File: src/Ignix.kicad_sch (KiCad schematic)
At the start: 13 parts, among them M1 Motor_DC, Q1 NPN, Q2 PNP, SW1 SW_Push

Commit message: revised repo
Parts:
- removed R2: 47kΩ, Resistor_THT:R_Axial_DIN0207_L6.3mm_D2.5mm_P7.62mm_Horizontal, symbol Device:R
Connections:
- net at M1.1 (+), Q2.1 (C): no longer D1.2 (A)
- net at BT1.1 (+), C1.2, Q1.3 (E)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: no longer M1.2 (-)
- new net: D1.2 (A), M1.2 (-)
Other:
- moved on the sheet: D1, M1, R5

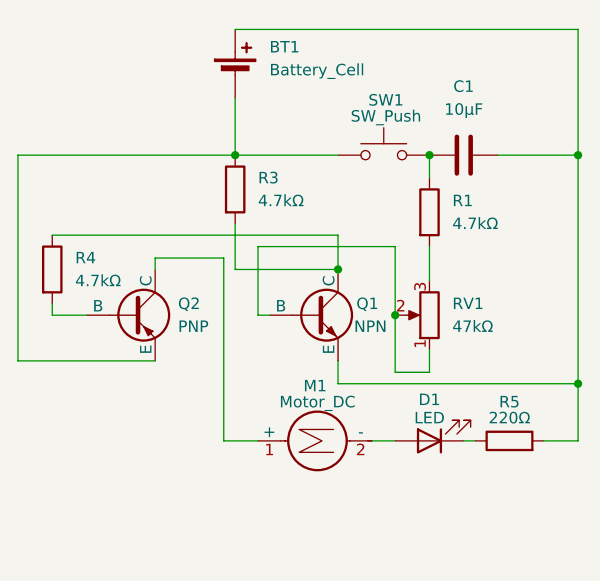
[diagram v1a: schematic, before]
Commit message: flipped battery
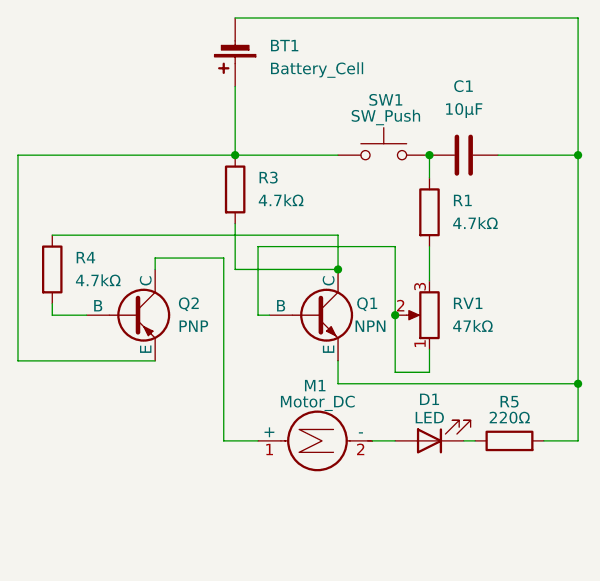
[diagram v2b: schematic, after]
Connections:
- net at C1.2, Q1.3 (E), R5.2: now also BT1.2 (-); no longer BT1.1 (+)
- net at Q2.3 (E), R3.1, SW1.1: now also BT1.1 (+); no longer BT1.2 (-)
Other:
- moved on the sheet: BT1
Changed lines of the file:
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@@
 	(wire
 		(pts
-			(xy 138.43 76.2) (xy 100.33 76.2)
+			(xy 138.43 74.93) (xy 100.33 74.93)
 		)
 		(stroke
@@
 	(wire
 		(pts
-			(xy 138.43 90.17) (xy 138.43 76.2)
+			(xy 138.43 90.17) (xy 138.43 74.93)
 		)
 		(stroke
@@
 	(wire
 		(pts
+			(xy 100.33 82.55) (xy 100.33 90.17)
+		)
+		(stroke
+			(width 0)
+			(type default)
+		)
+	)
+	(wire
+		(pts
 			(xy 91.44 101.6) (xy 91.44 102.87)
 		)
@@
 		(pts
 			(xy 121.92 92.71) (xy 121.92 90.17)
-		)
-		(stroke
-			(width 0)
-			(type default)
-		)
-	)
-	(wire
-		(pts
-			(xy 100.33 83.82) (xy 100.33 90.17)
 		)
 		(stroke
@@
 	(symbol
 		(lib_id "Device:Battery_Cell")
-		(at 100.33 81.28 0)
+		(at 100.33 77.47 180)
 		(unit 1)
 		(exclude_from_sim no)
@@
 		(fields_autoplaced yes)
 		(property "Reference" "BT1"
-			(at 104.14 78.1684 0)
-			(effects
-				(font
-					(size 1.27 1.27)
-				)
-				(justify left)
+			(at 104.14 78.0414 0)
+			(effects
+				(font
+					(size 1.27 1.27)
+				)
+				(justify right)
 			)
 		)
 		(property "Value" "Battery_Cell"
-			(at 104.14 80.7084 0)
-			(effects
-				(font
-					(size 1.27 1.27)
-				)
-				(justify left)
+			(at 104.14 80.5814 0)
+			(effects
+				(font
+					(size 1.27 1.27)
+				)
+				(justify right)
 			)
 		)
 		(property "Footprint" "Battery:BatteryHolder_Keystone_3034_1x20mm"
-			(at 100.33 79.756 90)
+			(at 100.33 78.994 90)
 			(effects
 				(font
@@
 		)
 		(property "Datasheet" "~"
-			(at 100.33 79.756 90)
+			(at 100.33 78.994 90)
 			(effects
 				(font
@@
 		)
 		(property "Description" "Single-cell battery"
-			(at 100.33 81.28 0)
-			(effects
-				(font
+			(at 100.33 77.47 0)
+			(effects
+				(font
